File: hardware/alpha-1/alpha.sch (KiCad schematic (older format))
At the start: 27 parts, among them P1 Conn_02x20_Odd_Even

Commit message: o Completing all TODOs for schematic.
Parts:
- removed D?: S1MTR, Diodes_SMD:D_SMA_Handsoldering, symbol D
- removed P?: SWITCH_3, Bitraf:PhoenixContact_PTSM0,5_2-2,5-H_SMD, symbol Conn_01x02
- removed Q?: DMN2041L-7, TO_SOT_Packages_SMD:SOT-23, symbol Q_NMOS_GDS
- removed R?: 10k, Resistors_SMD:R_0805, symbol R
- added D1, D11, D5, D7, D9: S1MTR, Diodes_SMD:D_SMA_Handsoldering, symbol D
- added D10, D12, D2, D4, D6, D8: LED, symbol LED
- added D14, D15, D16, D17, D18, D19, D20: D_Zener, symbol D_Zener
- added D21, D22, D23: LED, IPC7351-Most:LEDC3216X110, symbol LED
- added J1: POWER, Pin_Headers:Pin_Header_Straight_2x02_Pitch2.54mm, symbol Conn_02x02_Odd_Even
- added J2: SERIAL, Pin_Headers:Pin_Header_Straight_1x05_Pitch2.54mm, symbol Conn_01x05
- added P1: SWITCH_1, Bitraf:PhoenixContact_PTSM0,5_2-2,5-H_SMD, symbol Conn_01x02
- added P3: SWITCH_3, Bitraf:PhoenixContact_PTSM0,5_2-2,5-H_SMD, symbol Conn_01x02
- added P4: SWITCH_4, Bitraf:PhoenixContact_PTSM0,5_2-2,5-H_SMD, symbol Conn_01x02
- added P5: SWITCH_5, Bitraf:PhoenixContact_PTSM0,5_2-2,5-H_SMD, symbol Conn_01x02
- added P6: SWITCH_6, Bitraf:PhoenixContact_PTSM0,5_2-2,5-H_SMD, symbol Conn_01x02
- added Q1, Q3, Q4, Q5, Q6: DMN2041L-7, TO_SOT_Packages_SMD:SOT-23, symbol Q_NMOS_GSD
- added R1: 10k, IPC7351-Most:CAPC3216X70, symbol R
- added R10, R12, R2, R4, R6, R8: 270, symbol R
- added R11, R5, R7, R9: 10k, Resistors_SMD:R_0805, symbol R
- added R14, R15, R16, R17, R18, R19, R20: 10k, symbol R
- added R23, R27, R28: 560, symbol R
- added R24, R25, R26: R, symbol R
- added U2: TMP102, symbol TMP102
- P2: renamed from P?; value SWITCH_3 -> SWITCH_2
- P7: renamed from P?; value SWITCH_3 -> INPUTS; footprint Bitraf:PhoenixContact_PTSM0,5_2-2,5-H_SMD -> (none); symbol Conn_01x02 -> Conn_01x08
- P8: renamed from P1; value Conn_02x20_Odd_Even -> RASPBERRY_PI
- Q2: renamed from Q?; symbol Q_NMOS_GDS -> Q_NMOS_GSD
- gave numbers to parts that had none: 15
- renumbered MK3 to MK2, MK2 to MK3
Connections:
- net labels added: INPUT_2, INPUT_3, INPUT_4, INPUT_5, INPUT_6, INPUT_7, INPUT_8, SWITCH_1, SWITCH_3, SWITCH_4, SWITCH_5, SWITCH_6
- wire segments 128 -> 253
- no-connect marks 1 -> 3
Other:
- note added: "Inputs"
- note added: "Optionally powered by a GPIO pin to reduce self-heating.\n"
- note added: "Outputs"
- note added: "Power ports"
- note added: "Serial port"
- note added: "Status LEDs"
- note added: "TODO: extension header hvis lett\n"
- note added: "Temperature"
- note removed: "ID_SD and ID_SC PINS:\nThese pins are reserved for HAT ID EEPROM.\n\nAt boot time this I2C interface will be\ninterrogated to look for an EEPROM\nthat identifes the attached board and\nallows automagic setup of the GPIOs\n(and optionally, Linux drivers).\n\nDO NOT USE these pins for anything other\nthan attaching an I2C ID EEPROM. Leave\nunconnected if ID EEPROM not required."
- moved on the sheet: C1, C2, C3, C4, C5, C6, D13, D3, L1, MK1, MK2, MK3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

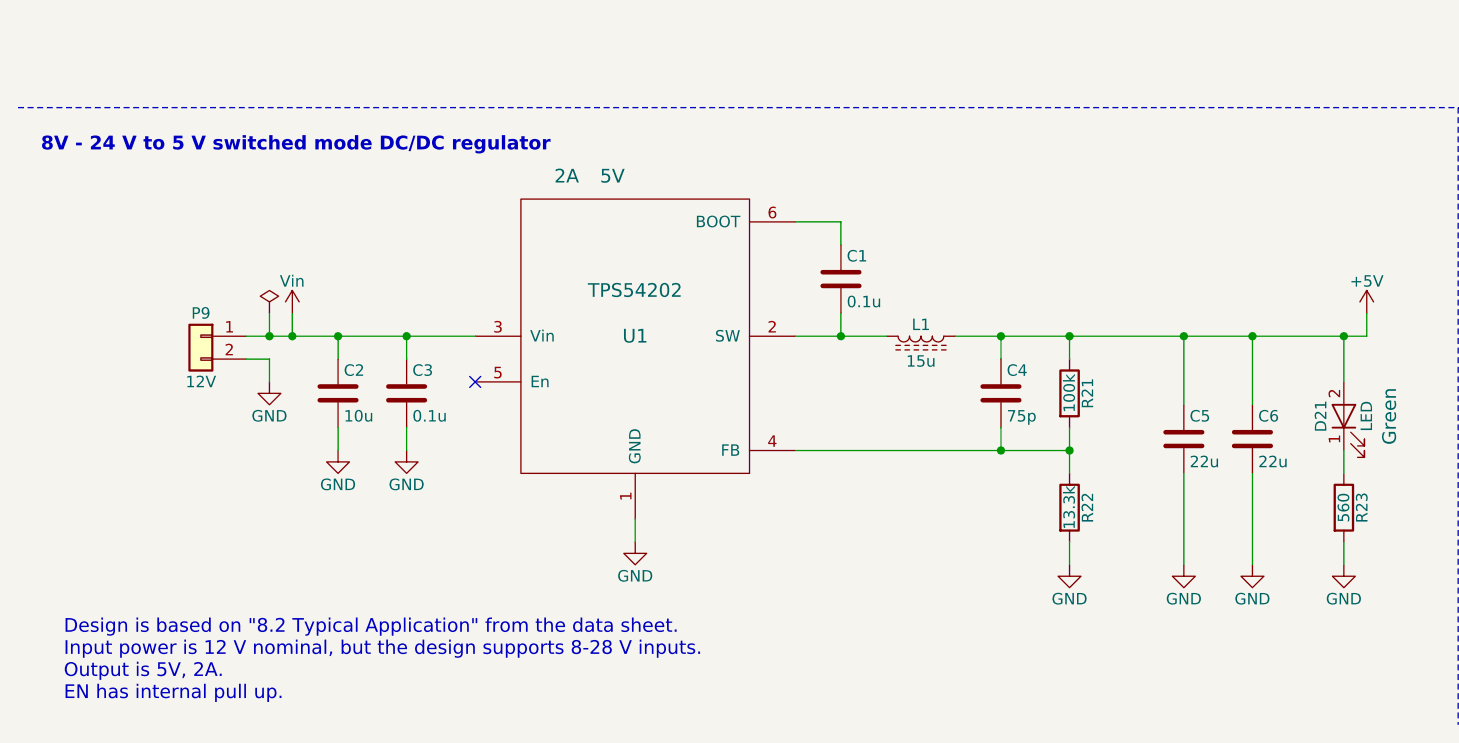
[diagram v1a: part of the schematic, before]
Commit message: o Refreshing DC/DC converter schematic from Bitraf's repository.
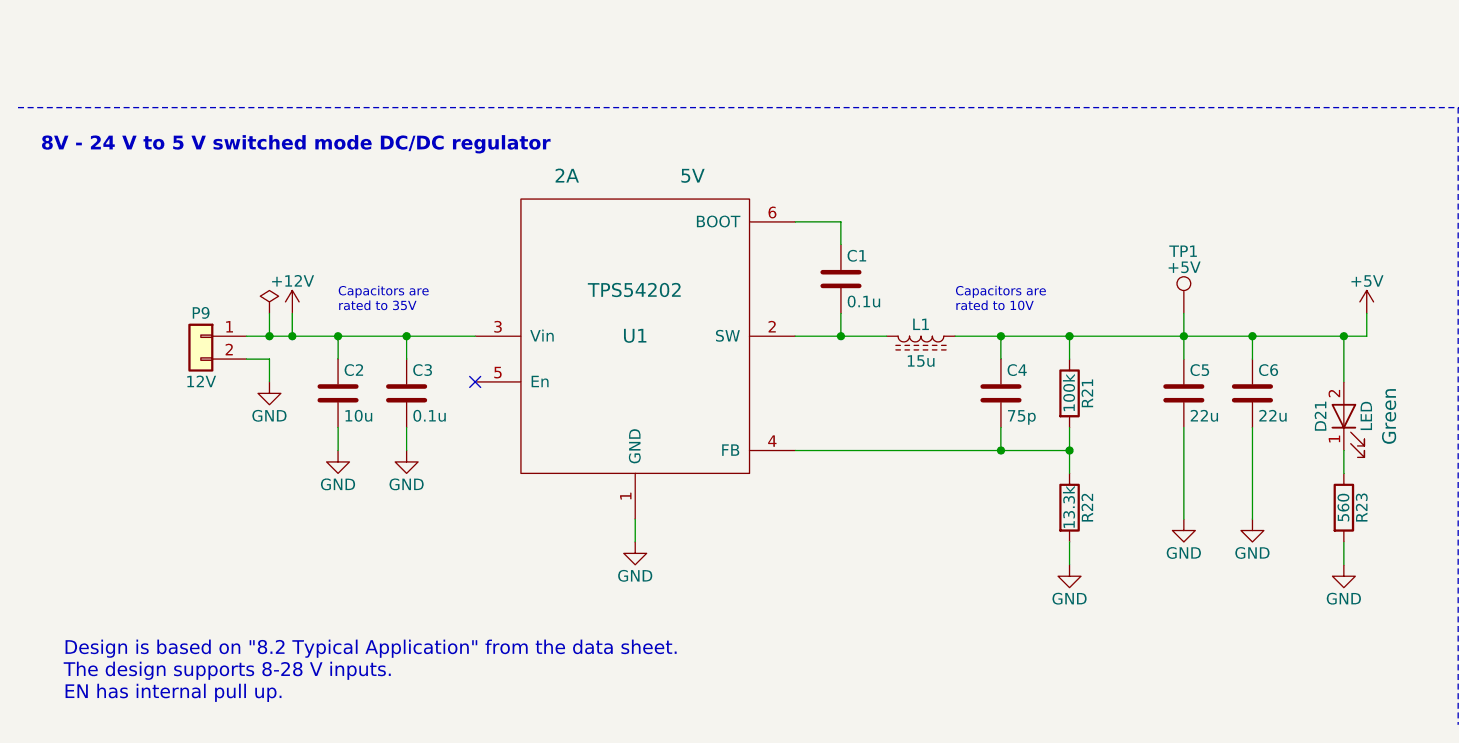
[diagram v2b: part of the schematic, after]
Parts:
- added TP1: +5V, Connectors_TestPoints:Test_Point_Pad_d1.0mm, symbol TEST_1P
- C1: mpn (none) -> CL21B104MBCNNNC; voltage (none) -> 10V
- C2: footprint Capacitors_SMD:C_0805 -> IPC7351-Nominal:CAPC3216X70; mpn (none) -> GMK212BBJ106KG-T; req_voltage (none) -> 35V
- C3: mpn (none) -> GMK212BJ104KGHT; req_voltage (none) -> 35V; ta_ref 0.1u -> (none); ta_value (none) -> 0.1u
- C4: mpn (none) -> 08051A750JAT2A; voltage (none) -> 10V
- C5, C6: mpn (none) -> CL21A226MQCLQNC; voltage (none) -> 10V
- P7: footprint (none) -> Bitraf:PhoenixContact_PTSM_0,5_8-2,5-H_SMD; mpn (none) -> 1771088
- P9: mpn (none) -> 1702473
- R21: mpn (none) -> RC0805FR-07100KL
- R22: mpn (none) -> RC0805FR-0713K3L
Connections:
- net +5V: now also TP1.1
- net Vin: no longer C2.1, C3.1, P9.1 (Pin_1), U1.3 (Vin)
- new net +12V: C2.1, C3.1, P9.1 (Pin_1), U1.3 (Vin)
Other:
- note added: "Capacitors are\nrated to 10V"
- note added: "Capacitors are\nrated to 35V"
- note added: "Design is based on "8.2 Typical Application" from the data sheet.\nThe design supports 8-28 V inputs.\nEN has internal pull up."
- note removed: "Design is based on "8.2 Typical Application" from the data sheet.\nInput power is 12 V nominal, but the design supports 8-28 V inputs.\nOutput is 5V, 2A.\nEN has internal pull up."

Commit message: o Laying out all components on PCB, updating footprints. Still some parts missing.
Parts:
- D21, D22, D23: footprint IPC7351-Most:LEDC3216X110 -> IPC7351-Nominal:LEDC3216X110
- P1, P2, P3, P4, P5, P6, P9: footprint Bitraf:PhoenixContact_PTSM0,5_2-2,5-H_SMD -> Bitraf:PhoenixContact_PTSM_0,5_2-2,5-H_SMD
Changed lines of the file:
@@
 F 0 "P2" H 9500 4100 50  0000 C CNN
 F 1 "SWITCH_2" H 9500 3800 50  0000 C CNN
-F 2 "Bitraf:PhoenixContact_PTSM0,5_2-2,5-H_SMD" H 9500 4000 50  0001 C CNN
+F 2 "Bitraf:PhoenixContact_PTSM_0,5_2-2,5-H_SMD" H 9500 4000 50  0001 C CNN
 F 3 "" H 9500 4000 50  0001 C CNN
 	1    9500 4000
@@
 F 0 "D21" H 6300 9850 50  0000 C CNN
 F 1 "LED" H 6300 9650 50  0000 C CNN
-F 2 "IPC7351-Most:LEDC3216X110" H 6300 9750 50  0001 C CNN
+F 2 "IPC7351-Nominal:LEDC3216X110" H 6300 9750 50  0001 C CNN
 F 3 "" H 6300 9750 50  0001 C CNN
 F 4 "Green" H 6300 9550 60  0000 C CNN "color"
@@
 F 0 "P1" H 9500 2100 50  0000 C CNN
 F 1 "SWITCH_1" H 9500 1800 50  0000 C CNN
-F 2 "Bitraf:PhoenixContact_PTSM0,5_2-2,5-H_SMD" H 9500 2000 50  0001 C CNN
+F 2 "Bitraf:PhoenixContact_PTSM_0,5_2-2,5-H_SMD" H 9500 2000 50  0001 C CNN
 F 3 "" H 9500 2000 50  0001 C CNN
 	1    9500 2000
@@
 F 0 "D23" H 11400 9350 50  0000 C CNN
 F 1 "LED" H 11400 9150 50  0000 C CNN
-F 2 "IPC7351-Most:LEDC3216X110" H 11400 9250 50  0001 C CNN
+F 2 "IPC7351-Nominal:LEDC3216X110" H 11400 9250 50  0001 C CNN
 F 3 "" H 11400 9250 50  0001 C CNN
 F 4 "Green" H 11400 9050 60  0000 C CNN "color"
@@
 F 0 "D22" H 10900 9350 50  0000 C CNN
 F 1 "LED" H 10900 9150 50  0000 C CNN
-F 2 "IPC7351-Most:LEDC3216X110" H 10900 9250 50  0001 C CNN
+F 2 "IPC7351-Nominal:LEDC3216X110" H 10900 9250 50  0001 C CNN
 F 3 "" H 10900 9250 50  0001 C CNN
 F 4 "Green" H 10900 9050 60  0000 C CNN "color"
@@
 F 0 "P3" H 9500 6100 50  0000 C CNN
 F 1 "SWITCH_3" H 9500 5800 50  0000 C CNN
-F 2 "Bitraf:PhoenixContact_PTSM0,5_2-2,5-H_SMD" H 9500 6000 50  0001 C CNN
+F 2 "Bitraf:PhoenixContact_PTSM_0,5_2-2,5-H_SMD" H 9500 6000 50  0001 C CNN
 F 3 "" H 9500 6000 50  0001 C CNN
 	1    9500 6000
@@
 F 0 "P4" H 11900 2100 50  0000 C CNN
 F 1 "SWITCH_4" H 11900 1800 50  0000 C CNN
-F 2 "Bitraf:PhoenixContact_PTSM0,5_2-2,5-H_SMD" H 11900 2000 50  0001 C CNN
+F 2 "Bitraf:PhoenixContact_PTSM_0,5_2-2,5-H_SMD" H 11900 2000 50  0001 C CNN
 F 3 "" H 11900 2000 50  0001 C CNN
 	1    11900 2000
@@
 F 0 "P5" H 11900 4100 50  0000 C CNN
 F 1 "SWITCH_5" H 11900 3800 50  0000 C CNN
-F 2 "Bitraf:PhoenixContact_PTSM0,5_2-2,5-H_SMD" H 11900 4000 50  0001 C CNN
+F 2 "Bitraf:PhoenixContact_PTSM_0,5_2-2,5-H_SMD" H 11900 4000 50  0001 C CNN
 F 3 "" H 11900 4000 50  0001 C CNN
 	1    11900 4000
@@
 F 0 "P6" H 11900 6100 50  0000 C CNN
 F 1 "SWITCH_6" H 11900 5800 50  0000 C CNN
-F 2 "Bitraf:PhoenixContact_PTSM0,5_2-2,5-H_SMD" H 11900 6000 50  0001 C CNN
+F 2 "Bitraf:PhoenixContact_PTSM_0,5_2-2,5-H_SMD" H 11900 6000 50  0001 C CNN
 F 3 "" H 11900 6000 50  0001 C CNN
 	1    11900 6000
@@
 F 0 "P9" H 1300 9500 50  0000 C CNN
 F 1 "12V" H 1300 9200 50  0000 C CNN
-F 2 "Bitraf:PhoenixContact_PTSM0,5_2-2,5-H_SMD" H 1300 9400 50  0001 C CNN
+F 2 "Bitraf:PhoenixContact_PTSM_0,5_2-2,5-H_SMD" H 1300 9400 50  0001 C CNN
 F 3 "" H 1300 9400 50  0001 C CNN
 F 4 "1702473" H 1300 9400 60  0001 C CNN "mpn"

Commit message: o More footprints.
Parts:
- C2: footprint IPC7351-Nominal:CAPC3216X70 -> IPC7351-Nominal:CAPC2012X70
- D1, D11, D3, D5, D7, D9: digikey (none) -> 1655-1506-2-ND; mpn (none) -> S1MTR
- R1: footprint IPC7351-Most:CAPC3216X70 -> IPC7351-Nominal:RESC1005X38
- R10, R12, R13, R14, R15, R16, R17, R18, R19, R2, R20, R27, R28, R4, R6, R8: footprint (none) -> IPC7351-Nominal:RESC1005X38
- R11, R3, R5, R7, R9: footprint Resistors_SMD:R_0805 -> IPC7351-Nominal:RESC1005X38
- R24, R25, R26: value R -> 10k; footprint (none) -> IPC7351-Nominal:RESC1005X38
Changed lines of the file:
@@
 F 0 "R3" V 8880 4850 50  0000 C CNN
 F 1 "10k" V 8800 4850 50  0000 C CNN
-F 2 "Resistors_SMD:R_0805" V 8730 4850 50  0001 C CNN
+F 2 "IPC7351-Nominal:RESC1005X38" V 8730 4850 50  0001 C CNN
 F 3 "" H 8800 4850 50  0000 C CNN
 	1    8800 4850
@@
 F 2 "Diodes_SMD:D_SMA_Handsoldering" H 9000 4050 50  0001 C CNN
 F 3 "http://www.smc-diodes.com/propdf/S1A-S1M%20N0560%20REV.B.pdf" H 9000 4050 50  0001 C CNN
+F 4 "S1MTR" H 9000 4050 60  0001 C CNN "mpn"
+F 5 "1655-1506-2-ND" H 9000 4050 60  0001 C CNN "digikey"
 	1    9000 4050
 	0    1    1    0
@@
 F 0 "R13" V 14830 1000 50  0000 C CNN
 F 1 "10k" V 14750 1000 50  0000 C CNN
-F 2 "" V 14680 1000 50  0001 C CNN
+F 2 "IPC7351-Nominal:RESC1005X38" V 14680 1000 50  0001 C CNN
 F 3 "" H 14750 1000 50  0001 C CNN
 	1    14750 1000
@@
 F 0 "R4" V 8630 5100 50  0000 C CNN
 F 1 "270" V 8550 5100 50  0000 C CNN
-F 2 "" V 8480 5100 50  0001 C CNN
+F 2 "IPC7351-Nominal:RESC1005X38" V 8480 5100 50  0001 C CNN
 F 3 "" H 8550 5100 50  0001 C CNN
 	1    8550 5100
@@
 F 0 "R1" V 8880 2850 50  0000 C CNN
 F 1 "10k" V 8800 2850 50  0000 C CNN
-F 2 "IPC7351-Most:CAPC3216X70" V 8730 2850 50  0001 C CNN
+F 2 "IPC7351-Nominal:RESC1005X38" V 8730 2850 50  0001 C CNN
 F 3 "" H 8800 2850 50  0000 C CNN
 	1    8800 2850
@@
 F 2 "Diodes_SMD:D_SMA_Handsoldering" H 9000 2050 50  0001 C CNN
 F 3 "http://www.smc-diodes.com/propdf/S1A-S1M%20N0560%20REV.B.pdf" H 9000 2050 50  0001 C CNN
+F 4 "S1MTR" H 9000 2050 60  0001 C CNN "mpn"
+F 5 "1655-1506-2-ND" H 9000 2050 60  0001 C CNN "digikey"
 	1    9000 2050
 	0    1    1    0
@@
 F 0 "R2" V 8630 3100 50  0000 C CNN
 F 1 "270" V 8550 3100 50  0000 C CNN
-F 2 "" V 8480 3100 50  0001 C CNN
+F 2 "IPC7351-Nominal:RESC1005X38" V 8480 3100 50  0001 C CNN
 F 3 "" H 8550 3100 50  0001 C CNN
 	1    8550 3100
@@
 F 0 "R28" V 11480 9650 50  0000 C CNN
 F 1 "560" V 11400 9650 50  0000 C CNN
-F 2 "" V 11330 9650 50  0001 C CNN
+F 2 "IPC7351-Nominal:RESC1005X38" V 11330 9650 50  0001 C CNN
 F 3 "" H 11400 9650 50  0001 C CNN
 	1    11400 9650
@@
 F 0 "R27" V 10980 9650 50  0000 C CNN
 F 1 "560" V 10900 9650 50  0000 C CNN
-F 2 "" V 10830 9650 50  0001 C CNN
+F 2 "IPC7351-Nominal:RESC1005X38" V 10830 9650 50  0001 C CNN
 F 3 "" H 10900 9650 50  0001 C CNN
 	1    10900 9650
@@
 F 0 "R14" V 14830 1900 50  0000 C CNN
 F 1 "10k" V 14750 1900 50  0000 C CNN
-F 2 "" V 14680 1900 50  0001 C CNN
+F 2 "IPC7351-Nominal:RESC1005X38" V 14680 1900 50  0001 C CNN
 F 3 "" H 14750 1900 50  0001 C CNN
 	1    14750 1900
@@
 F 0 "R15" V 14830 2800 50  0000 C CNN
 F 1 "10k" V 14750 2800 50  0000 C CNN
-F 2 "" V 14680 2800 50  0001 C CNN
+F 2 "IPC7351-Nominal:RESC1005X38" V 14680 2800 50  0001 C CNN
 F 3 "" H 14750 2800 50  0001 C CNN
 	1    14750 2800
@@
 F 0 "R16" V 14830 3600 50  0000 C CNN
 F 1 "10k" V 14750 3600 50  0000 C CNN
-F 2 "" V 14680 3600 50  0001 C CNN
+F 2 "IPC7351-Nominal:RESC1005X38" V 14680 3600 50  0001 C CNN
 F 3 "" H 14750 3600 50  0001 C CNN
 	1    14750 3600
@@
 F 0 "R17" V 14830 4500 50  0000 C CNN
 F 1 "10k" V 14750 4500 50  0000 C CNN
-F 2 "" V 14680 4500 50  0001 C CNN
+F 2 "IPC7351-Nominal:RESC1005X38" V 14680 4500 50  0001 C CNN
 F 3 "" H 14750 4500 50  0001 C CNN
 	1    14750 4500
@@
 F 0 "R5" V 8880 6850 50  0000 C CNN
 F 1 "10k" V 8800 6850 50  0000 C CNN
-F 2 "Resistors_SMD:R_0805" V 8730 6850 50  0001 C CNN
+F 2 "IPC7351-Nominal:RESC1005X38" V 8730 6850 50  0001 C CNN
 F 3 "" H 8800 6850 50  0000 C CNN
 	1    8800 6850
@@
 F 2 "Diodes_SMD:D_SMA_Handsoldering" H 9000 6050 50  0001 C CNN
 F 3 "http://www.smc-diodes.com/propdf/S1A-S1M%20N0560%20REV.B.pdf" H 9000 6050 50  0001 C CNN
+F 4 "S1MTR" H 9000 6050 60  0001 C CNN "mpn"
+F 5 "1655-1506-2-ND" H 9000 6050 60  0001 C CNN "digikey"
 	1    9000 6050
 	0    1    1    0
@@
 F 0 "R6" V 8630 7100 50  0000 C CNN
 F 1 "270" V 8550 7100 50  0000 C CNN
-F 2 "" V 8480 7100 50  0001 C CNN
+F 2 "IPC7351-Nominal:RESC1005X38" V 8480 7100 50  0001 C CNN
 F 3 "" H 8550 7100 50  0001 C CNN
 	1    8550 7100
@@
 F 0 "R7" V 11280 2850 50  0000 C CNN
 F 1 "10k" V 11200 2850 50  0000 C CNN
-F 2 "Resistors_SMD:R_0805" V 11130 2850 50  0001 C CNN
+F 2 "IPC7351-Nominal:RESC1005X38" V 11130 2850 50  0001 C CNN
 F 3 "" H 11200 2850 50  0000 C CNN
 	1    11200 2850
@@
 F 2 "Diodes_SMD:D_SMA_Handsoldering" H 11400 2050 50  0001 C CNN
 F 3 "http://www.smc-diodes.com/propdf/S1A-S1M%20N0560%20REV.B.pdf" H 11400 2050 50  0001 C CNN
+F 4 "S1MTR" H 11400 2050 60  0001 C CNN "mpn"
+F 5 "1655-1506-2-ND" H 11400 2050 60  0001 C CNN "digikey"
 	1    11400 2050
 	0    1    1    0
@@
 F 0 "R8" V 11030 3100 50  0000 C CNN
 F 1 "270" V 10950 3100 50  0000 C CNN
-F 2 "" V 10880 3100 50  0001 C CNN
+F 2 "IPC7351-Nominal:RESC1005X38" V 10880 3100 50  0001 C CNN
 F 3 "" H 10950 3100 50  0001 C CNN
 	1    10950 3100
@@
 P 8700 9350
 F 0 "R24" V 8780 9350 50  0000 C CNN
-F 1 "R" V 8700 9350 50  0000 C CNN
-F 2 "" V 8630 9350 50  0001 C CNN
+F 1 "10k" V 8700 9350 50  0000 C CNN
+F 2 "IPC7351-Nominal:RESC1005X38" V 8630 9350 50  0001 C CNN
 F 3 "" H 8700 9350 50  0001 C CNN
 	1    8700 9350
@@
 P 8900 9350
 F 0 "R25" V 8980 9350 50  0000 C CNN
-F 1 "R" V 8900 9350 50  0000 C CNN
-F 2 "" V 8830 9350 50  0001 C CNN
+F 1 "10k" V 8900 9350 50  0000 C CNN
+F 2 "IPC7351-Nominal:RESC1005X38" V 8830 9350 50  0001 C CNN
 F 3 "" H 8900 9350 50  0001 C CNN
 	1    8900 9350
@@
 P 9100 9350
 F 0 "R26" V 9180 9350 50  0000 C CNN
-F 1 "R" V 9100 9350 50  0000 C CNN
-F 2 "" V 9030 9350 50  0001 C CNN
+F 1 "10k" V 9100 9350 50  0000 C CNN
+F 2 "IPC7351-Nominal:RESC1005X38" V 9030 9350 50  0001 C CNN
 F 3 "" H 9100 9350 50  0001 C CNN
 	1    9100 9350
@@
 F 0 "R9" V 11280 4850 50  0000 C CNN
 F 1 "10k" V 11200 4850 50  0000 C CNN
-F 2 "Resistors_SMD:R_0805" V 11130 4850 50  0001 C CNN
+F 2 "IPC7351-Nominal:RESC1005X38" V 11130 4850 50  0001 C CNN
 F 3 "" H 11200 4850 50  0000 C CNN
 	1    11200 4850
@@
 F 2 "Diodes_SMD:D_SMA_Handsoldering" H 11400 4050 50  0001 C CNN
 F 3 "http://www.smc-diodes.com/propdf/S1A-S1M%20N0560%20REV.B.pdf" H 11400 4050 50  0001 C CNN
+F 4 "S1MTR" H 11400 4050 60  0001 C CNN "mpn"
+F 5 "1655-1506-2-ND" H 11400 4050 60  0001 C CNN "digikey"
 	1    11400 4050
 	0    1    1    0
@@
 F 0 "R10" V 11030 5100 50  0000 C CNN
 F 1 "270" V 10950 5100 50  0000 C CNN
-F 2 "" V 10880 5100 50  0001 C CNN
+F 2 "IPC7351-Nominal:RESC1005X38" V 10880 5100 50  0001 C CNN
 F 3 "" H 10950 5100 50  0001 C CNN
 	1    10950 5100
@@
 F 0 "R18" V 14830 5400 50  0000 C CNN
 F 1 "10k" V 14750 5400 50  0000 C CNN
-F 2 "" V 14680 5400 50  0001 C CNN
+F 2 "IPC7351-Nominal:RESC1005X38" V 14680 5400 50  0001 C CNN
 F 3 "" H 14750 5400 50  0001 C CNN
 	1    14750 5400
@@
 F 0 "R19" V 14830 6300 50  0000 C CNN
 F 1 "10k" V 14750 6300 50  0000 C CNN
-F 2 "" V 14680 6300 50  0001 C CNN
+F 2 "IPC7351-Nominal:RESC1005X38" V 14680 6300 50  0001 C CNN
 F 3 "" H 14750 6300 50  0001 C CNN
 	1    14750 6300
@@
 F 0 "R20" V 14830 7200 50  0000 C CNN
 F 1 "10k" V 14750 7200 50  0000 C CNN
-F 2 "" V 14680 7200 50  0001 C CNN
+F 2 "IPC7351-Nominal:RESC1005X38" V 14680 7200 50  0001 C CNN
 F 3 "" H 14750 7200 50  0001 C CNN
 	1    14750 7200
@@
 F 0 "R11" V 11280 6850 50  0000 C CNN
 F 1 "10k" V 11200 6850 50  0000 C CNN
-F 2 "Resistors_SMD:R_0805" V 11130 6850 50  0001 C CNN
+F 2 "IPC7351-Nominal:RESC1005X38" V 11130 6850 50  0001 C CNN
 F 3 "" H 11200 6850 50  0000 C CNN
 	1    11200 6850
@@
 F 2 "Diodes_SMD:D_SMA_Handsoldering" H 11400 6050 50  0001 C CNN
 F 3 "http://www.smc-diodes.com/propdf/S1A-S1M%20N0560%20REV.B.pdf" H 11400 6050 50  0001 C CNN
+F 4 "S1MTR" H 11400 6050 60  0001 C CNN "mpn"
+F 5 "1655-1506-2-ND" H 11400 6050 60  0001 C CNN "digikey"
 	1    11400 6050
 	0    1    1    0
@@
 F 0 "R12" V 11030 7100 50  0000 C CNN
 F 1 "270" V 10950 7100 50  0000 C CNN
-F 2 "" V 10880 7100 50  0001 C CNN
+F 2 "IPC7351-Nominal:RESC1005X38" V 10880 7100 50  0001 C CNN
 F 3 "" H 10950 7100 50  0001 C CNN
 	1    10950 7100
@@
 F 0 "C2" H 1925 9750 50  0000 L CNN
 F 1 "10u" H 1925 9550 50  0000 L CNN
-F 2 "IPC7351-Nominal:CAPC3216X70" H 1938 9500 50  0001 C CNN
+F 2 "IPC7351-Nominal:CAPC2012X70" H 1938 9500 50  0001 C CNN
 F 3 "" H 1900 9650 50  0000 C CNN
 F 4 "C1" H 1900 9650 60  0001 C CNN "ta_ref"

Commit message: o Refactoring schematic, moving inputs to the left, outputs to the right and the header in the middle.
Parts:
- D10, D12, D2, D4, D6, D8: footprint (none) -> IPC7351-Nominal:LEDC3216X110
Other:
- note added: "Mounting holes"
- note added: "Power"
- note added: "Serial port #0"
- note removed: "Mounting Holes"
- note removed: "Power ports"
- note removed: "Serial port"
- moved on the sheet: D1, D10, D11, D12, D13, D14, D15, D16, D17, D18, D19, D2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

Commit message: o Footprints should be complete, still missing some MPNs.
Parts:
- D13, D14, D15, D16, D17, D18, D19, D20: value D_Zener -> BZX384C4V7; footprint (none) -> smd-semi:SOD-323; mpn (none) -> BZX384C4V7-E3-08
- P1, P2, P3, P4, P5, P6: mpn (none) -> 1702473
- Q1, Q2, Q3, Q4, Q5, Q6: mpn (none) -> DMN2041L-7
- R23: footprint (none) -> IPC7351-Nominal:RESC1005X38
- U2: footprint (none) -> Bitraf:SOT-563; mpn (none) -> TMP102AIDRLT
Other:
- moved on the sheet: R13, R14, R15, R16, R17, R18, R19, R20
